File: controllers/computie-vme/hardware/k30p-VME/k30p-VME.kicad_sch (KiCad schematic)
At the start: 8 parts, among them J1 5V, J6 5V

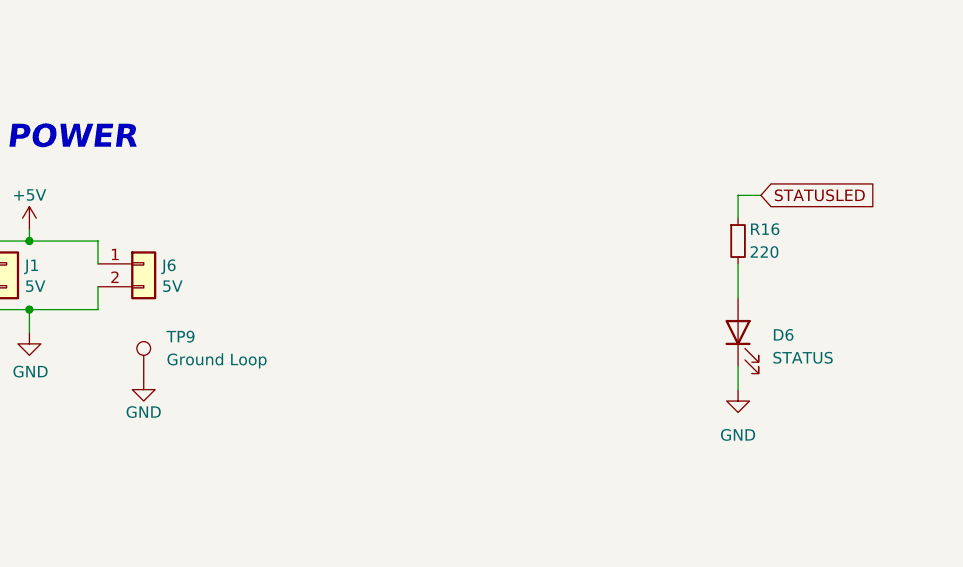
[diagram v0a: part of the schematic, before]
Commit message: Added SystemBoardSMT, renamed k30 boards, and added progress
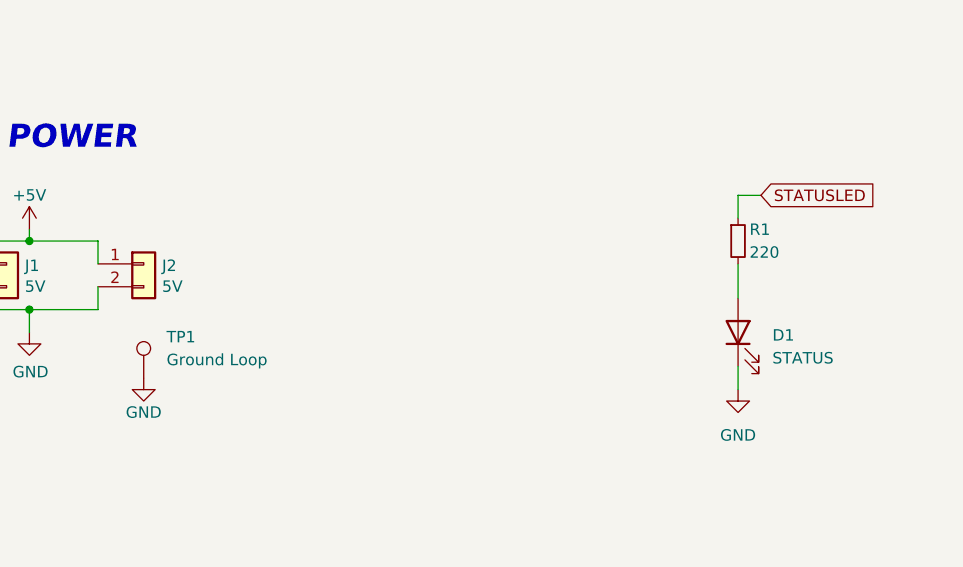
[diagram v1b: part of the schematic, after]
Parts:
- R1: renamed from R16; footprint Resistor_THT:R_Axial_DIN0204_L3.6mm_D1.6mm_P5.08mm_Horizontal -> Resistor_SMD:R_0805_2012Metric_Pad1.20x1.40mm_HandSolder
- renumbered D6 to D1, J6 to J2, TP9 to TP1
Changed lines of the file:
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@@
 		(dnp no)
 		(fields_autoplaced yes)
-		(property "Reference" "TP9"
+		(property "Reference" "TP1"
 			(at 109.22 130.048 0)
 			(effects
@@
 			(project "k30p-VME16"
 				(path "/dd13a6b9-cb24-4a73-96ce-c29930072fba"
-					(reference "TP9")
+					(reference "TP1")
 					(unit 1)
 				)
@@
 		(dnp no)
 		(fields_autoplaced yes)
-		(property "Reference" "D6"
+		(property "Reference" "D1"
 			(at 176.53 129.8574 90)
 			(effects
@@
 			(project "k30p-VME16"
 				(path "/dd13a6b9-cb24-4a73-96ce-c29930072fba"
-					(reference "D6")
+					(reference "D1")
 					(unit 1)
 				)
@@
 		(on_board yes)
 		(dnp no)
-		(property "Reference" "J6"
+		(property "Reference" "J2"
 			(at 108.712 122.1232 0)
 			(effects
@@
 			(project "k30p-VME16"
 				(path "/dd13a6b9-cb24-4a73-96ce-c29930072fba"
-					(reference "J6")
+					(reference "J2")
 					(unit 1)
 				)
@@
 		(dnp no)
 		(fields_autoplaced yes)
-		(property "Reference" "#PWR079"
+		(property "Reference" "#PWR04"
 			(at 172.72 142.24 0)
 			(effects
@@
 			(project "k30p-VME16"
 				(path "/dd13a6b9-cb24-4a73-96ce-c29930072fba"
-					(reference "#PWR079")
+					(reference "#PWR04")
 					(unit 1)
 				)
@@
 		(on_board yes)
 		(dnp no)
-		(property "Reference" "#PWR010"
+		(property "Reference" "#PWR01"
 			(at 93.98 121.92 0)
 			(effects
@@
 			(project "k30p-VME16"
 				(path "/dd13a6b9-cb24-4a73-96ce-c29930072fba"
-					(reference "#PWR010")
+					(reference "#PWR01")
 					(unit 1)
 				)
@@
 		(on_board yes)
 		(dnp no)
-		(property "Reference" "#PWR078"
+		(property "Reference" "#PWR03"
 			(at 106.68 140.97 0)
 			(effects
@@
 			(project "k30p-VME16"
 				(path "/dd13a6b9-cb24-4a73-96ce-c29930072fba"
-					(reference "#PWR078")
+					(reference "#PWR03")
 					(unit 1)
 				)
@@
 		(on_board yes)
 		(dnp no)
-		(property "Reference" "R16"
+		(property "Reference" "R1"
 			(at 173.99 118.11 0)
 			(effects
@@
 			)
 		)
-		(property "Footprint" "Resistor_THT:R_Axial_DIN0204_L3.6mm_D1.6mm_P5.08mm_Horizontal"
+		(property "Footprint" "Resistor_SMD:R_0805_2012Metric_Pad1.20x1.40mm_HandSolder"
 			(at 172.72 119.38 0)
 			(effects
@@
 			(project "k30p-VME16"
 				(path "/dd13a6b9-cb24-4a73-96ce-c29930072fba"
-					(reference "R16")
+					(reference "R1")
 					(unit 1)
 				)
@@
 		(on_board yes)
 		(dnp no)
-		(property "Reference" "#PWR011"
+		(property "Reference" "#PWR02"
 			(at 93.98 135.89 0)
 			(effects
@@
 			(project "k30p-VME16"
 				(path "/dd13a6b9-cb24-4a73-96ce-c29930072fba"
-					(reference "#PWR011")
-					(unit 1)
-				)
+					(reference "#PWR02")
+					(unit 1)
+				)

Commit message: Updating with more work in progress
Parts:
- removed D1: STATUS, LED_THT:LED_D3.0mm, symbol Device:LED
- removed R1: 220, Resistor_SMD:R_0805_2012Metric_Pad1.20x1.40mm_HandSolder, symbol Device:R_Small
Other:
- title: k30-VME32 -> k30p-VME
- moved on the sheet: H1, H2, J1, J2, S1, TP1

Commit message: Reorganized a bit
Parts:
- removed H1, H2: MountingHole, MountingHole:MountingHole_2.7mm_M2.5_DIN965, symbol Mechanical:MountingHole
- added C2, C3: 18pF, Capacitor_THT:C_Disc_D3.0mm_W2.0mm_P2.50mm, symbol Device:C_Small
- added R5: 15k, Resistor_SMD:R_0805_2012Metric_Pad1.20x1.40mm_HandSolder, symbol Device:R
- added U2: 74HC14, Package_SO:TSSOP-14_4.4x5mm_P0.65mm, symbol 74xx:74HC14
- added Y1: Crystal, Crystal:Crystal_HC49-4H_Vertical, symbol Device:Crystal
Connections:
- net GND: now also C2.2, C3.2
- new net: C2.1, R5.2, U2.3, Y1.1
- new net: C3.1, R5.1, U2.4, U2.5, Y1.2
- new net MAIN_CLK: U2.6
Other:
- note added: "MAIN CLOCK"
- moved on the sheet: S1

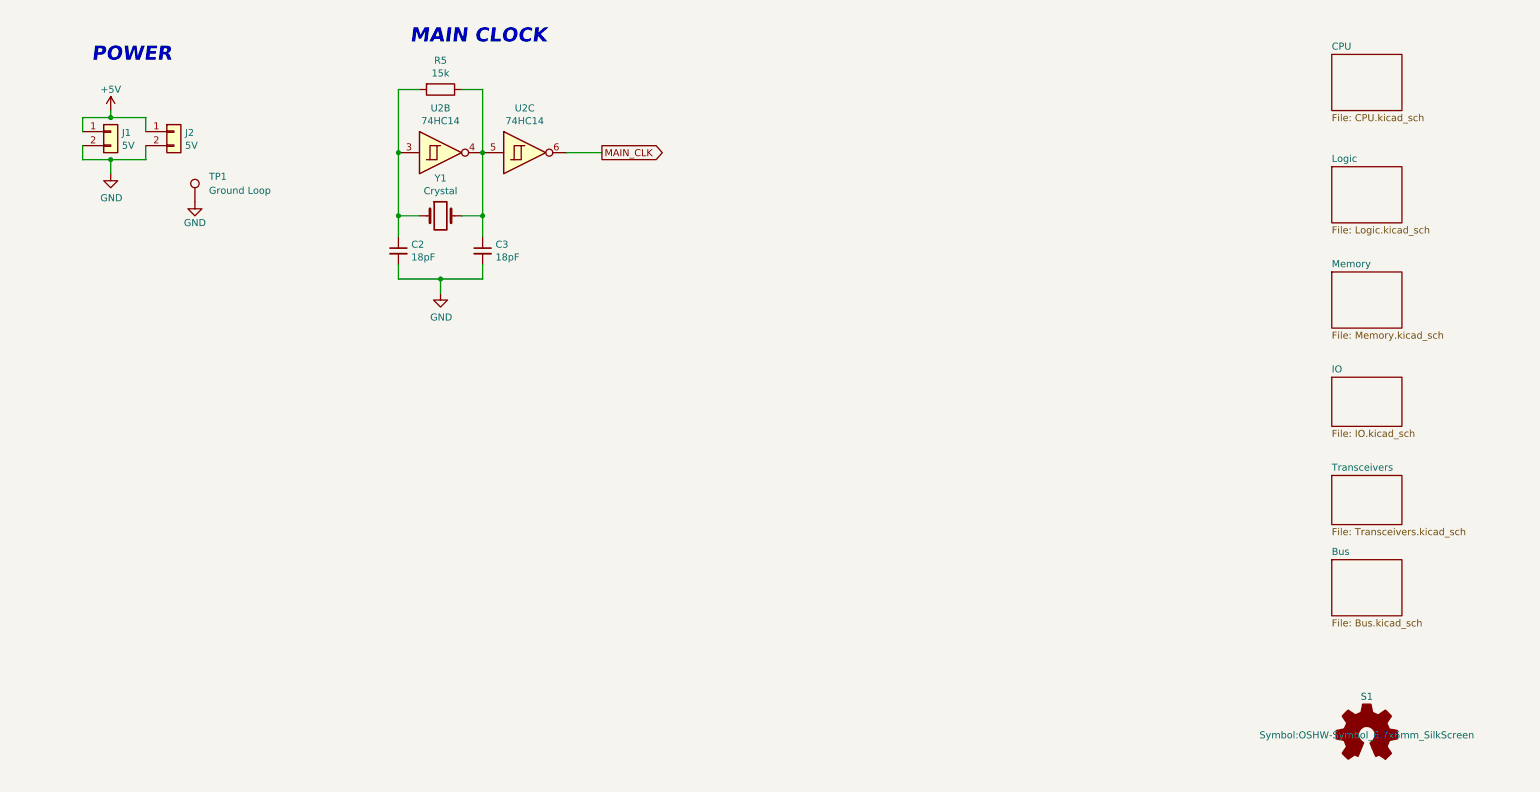
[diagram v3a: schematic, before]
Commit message: Basic systemboard logic for bus arbitration is working and tested
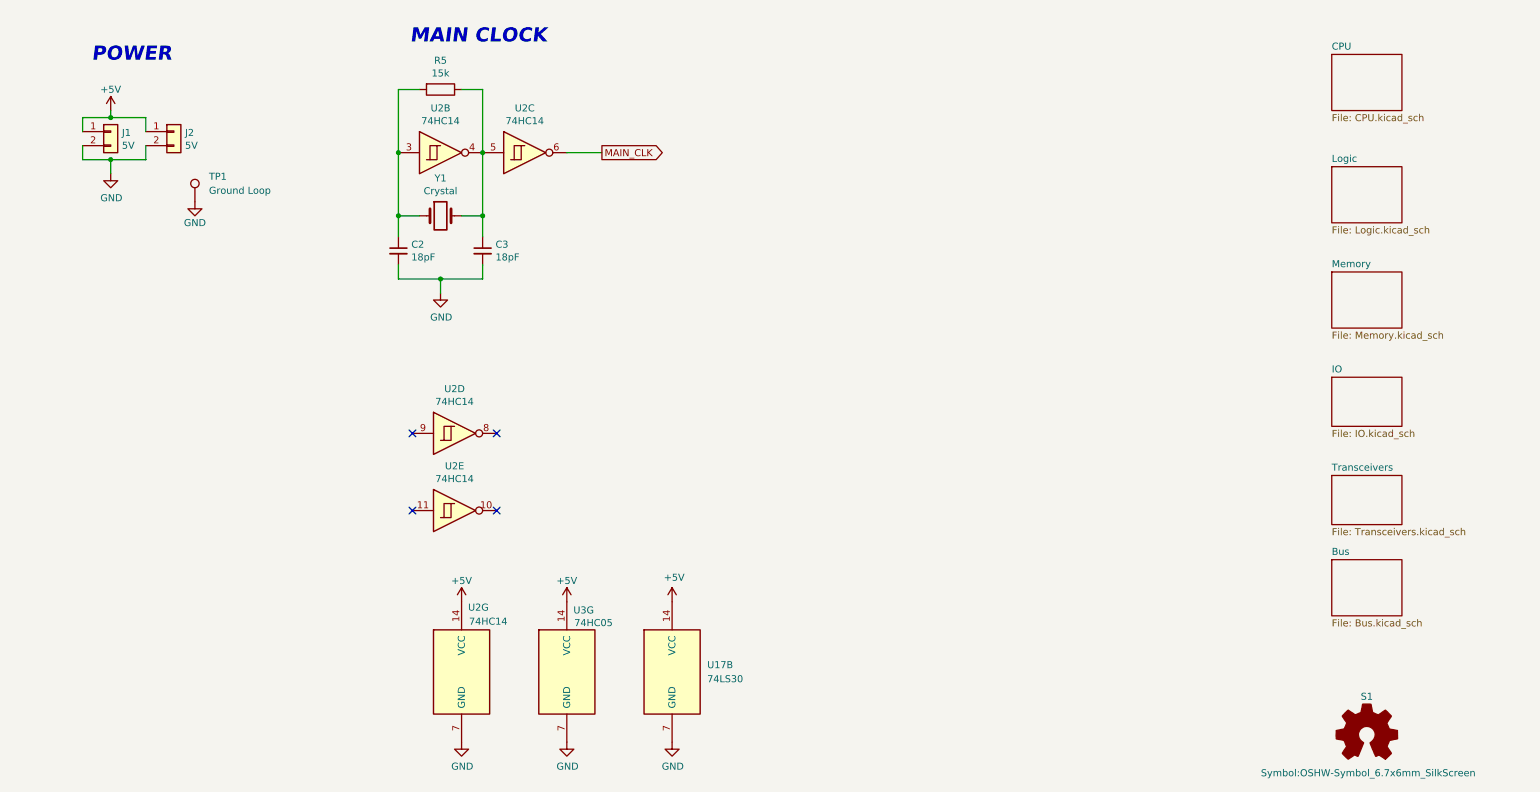
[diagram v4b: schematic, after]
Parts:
- added U17: 74LS30, symbol 74xx:74LS30
- added unit 4 of U2
- added unit 7 of U2
- added unit 5 of U2
- added U3: 74HC05, Package_SO:TSSOP-14_4.4x5mm_P0.65mm, symbol 74xx:74LS05
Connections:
- net +5V: now also U17.14 (VCC), U2.14 (VCC), U3.14 (VCC)
- net GND: now also U17.7 (GND), U2.7 (GND), U3.7 (GND)
- no-connect marks 0 -> 4

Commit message: Schematics for k30p-VME more or less done
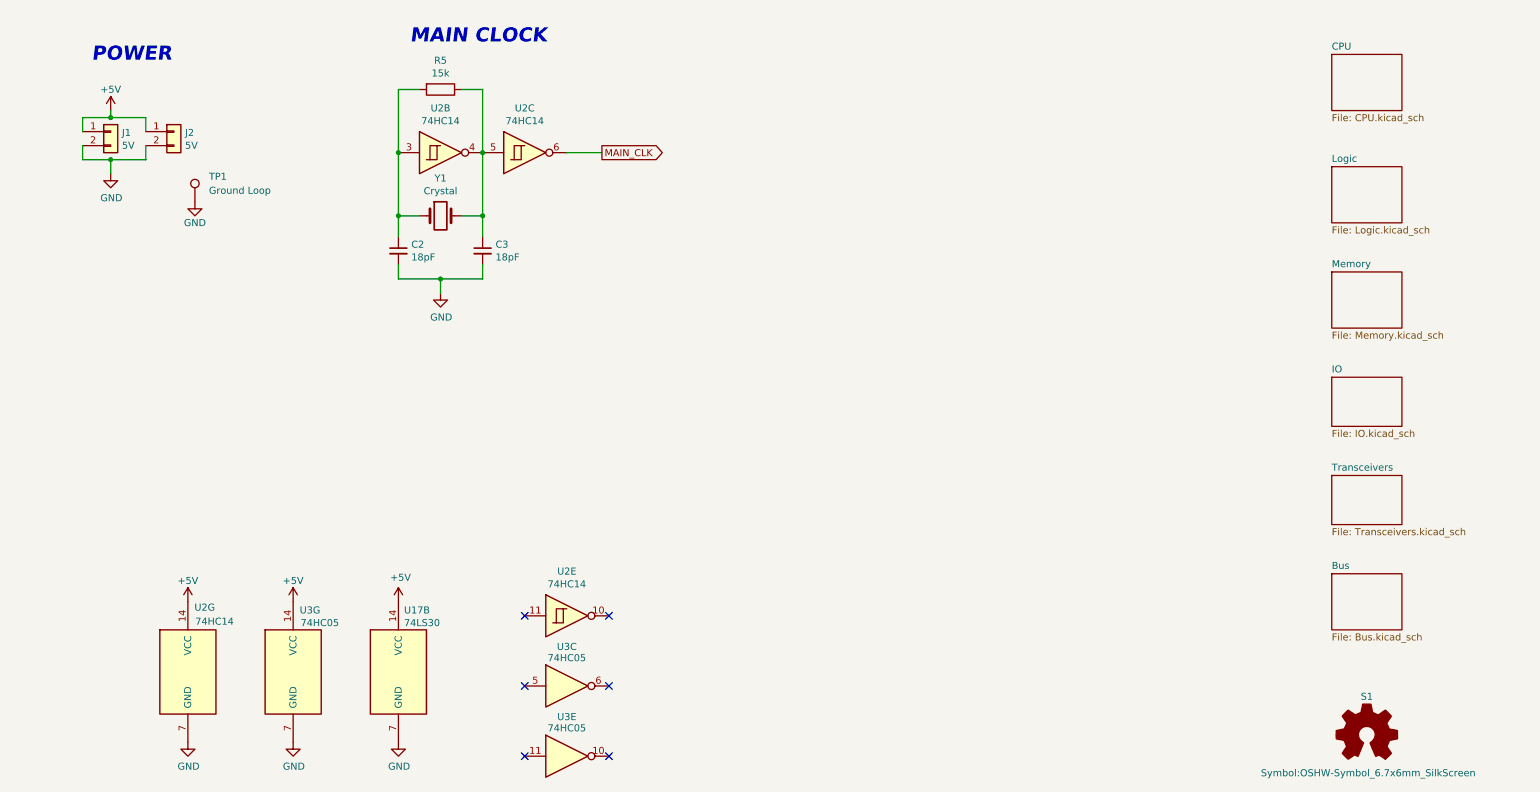
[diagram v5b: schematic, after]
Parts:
- removed unit 4 of U2
- added unit 3 of U3
- added unit 5 of U3
- U17: footprint (none) -> Package_SO:TSSOP-14_4.4x5mm_P0.65mm
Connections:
- no-connect marks 4 -> 6
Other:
- moved on the sheet: U17B, U2E, U2G, U3G

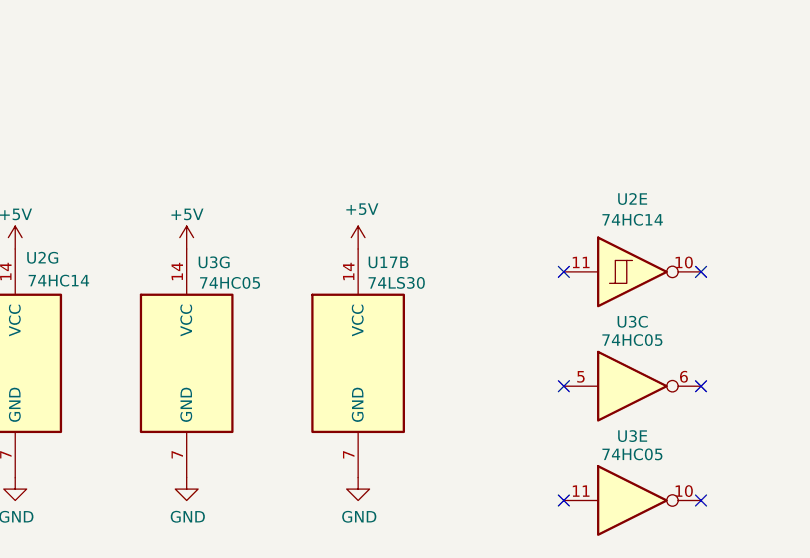
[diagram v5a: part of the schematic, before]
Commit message: Added MemBird - Woodcock (16-bit VME memory card)
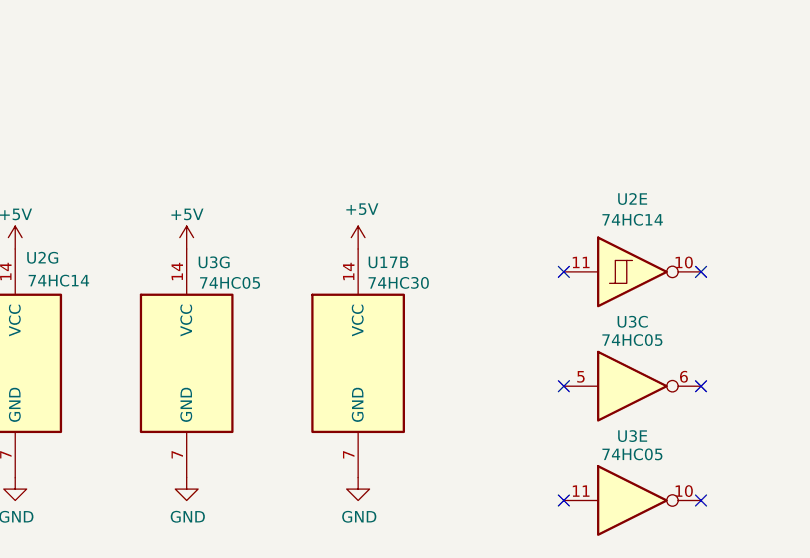
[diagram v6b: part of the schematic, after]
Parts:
- U17: value 74LS30 -> 74HC30
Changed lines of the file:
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@@
 			)
 		)
-		(property "Value" "74LS30"
+		(property "Value" "74HC30"
 			(at 84.836 129.54 0)
 			(effects
